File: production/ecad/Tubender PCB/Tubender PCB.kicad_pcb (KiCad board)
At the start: 4 copper layers, 352.2 x 159.2 mm, 262 parts, among them IC1 74HC4050D, IC2 RA8875L3N, IC3 CD4051BM96, IC4 CD4051BM96, J1 640387-2, J10 640387-2, J10 640387-5, J11 640387-8, J12 640387-2, J13 640387-5, J14 640387-3, J15 640387-2, J16 640387-2, J17 640387-2, J18 640387-2, J19 640387-2, J2 640387-5, J20 640387-2, J21 640387-2, J22 640387-2, J23 640387-2, J24 640387-2, J25 640387-2, J26 640387-2, J27 640387-2, J28 640387-2, J29 1-640387-0, J3 640387-5, J30 640387-2, J31 640387-5, J32 USB4110GFA, J33 640387-2, J34 640387-2, J35 640387-3, J37 640387-3, J4 640387-5, J5 640387-2, J5 640387-6, J6 640387-2, J6 640387-6, J7 4-1734592-0, J8 640387-3, J8 640387-6, J9 640387-3, J9 640387-5, Q1 AO3400A, Q2 AO3400A, U1 LMR36520FADDAR, U10 MCP23017-E_SO, U11 SN74AHC1G125DBVR, U12 LM5146RGYR, U13 LM5017SDX/NOPB, U2 ESP32-WROOM-32UE_M113EH6400UH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, U3 MCP23017-E_SO, U5 TPSM265R1V5SILR, U6 CP2102N-A02-GQFN28, Y1 ABM8-20.000MHz-10-B1U-T

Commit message: ok
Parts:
- CBOOT33: value 0.1u -> 0.1uF
- C_BST3, C_VIN1: value 100n -> 100nF
- C_C1: value 6.8n -> 6.8nF
- C_C2: value 312p -> 312pF
- C_C3: value 1n -> 1nF
- C_HF33: value 220n -> 220nF
- C_ILIM1: value 3p -> 3pF
- C_IN2, C_IN33: value 4.7u -> 4.7uF
- C_OUT3: value 10u -> 10uF
- C_OUT33: value 100u -> 100uF
- C_SS1: value 12.5n -> 12.5nF
- C_VCC2: value 2.2u -> 2.2uF
- C_VCC33: value 1u -> 1uF
- L1: value 8.5u -> 8.5uH
- L2: value 12u -> 12uH
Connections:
- U12 pad 22: GND -> (no net)
- U12 pad 23: GND -> (no net)
- U12 pad 24: GND -> (no net)
- U12 pad 25: GND -> (no net)
- U5 pad V: GND -> (no net)
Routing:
- net GND: track 479.9 -> 470.3 mm, vias 87 -> 88
- net ROTATION_ENA+: track 169.1 -> 164.6 mm
- net GPIO_0: track 117.8 -> 115.5 mm, vias 3 -> 2
- net DISPLAY_INT: track 126.3 -> 124.2 mm
- net 24V: track 541.8 -> 540.8 mm
- net TOUCH_XN: track 57.5 -> 56.7 mm
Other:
- board text added: "12V TP"
- board text added: "24V TP"
- board text added: "48V TP"
- board text added: "5V TP"

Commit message: lfg!!!
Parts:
- added G***: LOGO, LOGO, F.Cu at (368.1, 215.0)
- added G***: LOGO, LOGO, F.Cu at (44.2, 79.0)
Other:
- board text added: "(TUBENDER PCB BY NIK AND ETHAN) (SHOUTOUT MAGGIE, NIKI, MATT AND SEAN)"
- board text added: "TUBENDER!!!!!"

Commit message: Duplicate Connectors on Main PCB
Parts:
- removed the J10 at (361.6, 140.1)
- removed the J5 at (361.6, 200.9)
- removed the J6 at (361.6, 170.1)
- removed the J9 at (361.6, 116.7)
- C19, C20, C21, C22, C23, C24, C25, C26, C27, C28, C29, C30, C31, C32, C33: value 500nF -> 490nF
- C_OUT12: value 22u -> 22uF
- moved R8 160.4 mm to (213.4, 94.7)
- moved R18 134.5 mm to (224.2, 90.4), turned to 0 degrees
- moved R7 130.4 mm to (266.4, 90.7), turned to 0 degrees
- moved R17 98.0 mm to (284.2, 90.2), turned to 180 degrees
- moved G*** 55.5 mm to (359.3, 160.2)
- moved R45 43.9 mm to (347.7, 91.7)
- moved R44 40.5 mm to (350.7, 90.8), turned to 0 degrees
- moved R67 26.7 mm to (369.0, 84.3)
- moved G*** 0.51 mm to (44.3, 79.5)
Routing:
- net DIE_LIMIT_2: track 171.0 -> 44.6 mm, vias 3 -> 2
- net DIE_LIMIT_1: track 173.6 -> 48.8 mm, vias 3 -> 2
- net 12V: track 372.5 -> 249.0 mm
- net ADVANCE_LIMIT_1: track 219.2 -> 97.0 mm, vias 3 -> 2
- net ADVANCE_LIMIT_2: track 177.7 -> 56.3 mm, vias 4 -> 2
- net DIE_BEAM: track 191.8 -> 82.9 mm, vias 3 -> 2
- net CHUCK_BEAM: track 184.4 -> 147.5 mm, vias 2 -> 3
- net Net-(J32-CC2): track 33.3 -> 9.88 mm
- net 5V: track 618.8 -> 596.4 mm
- net GND: track 470.3 -> 489.6 mm, vias 88 -> 86

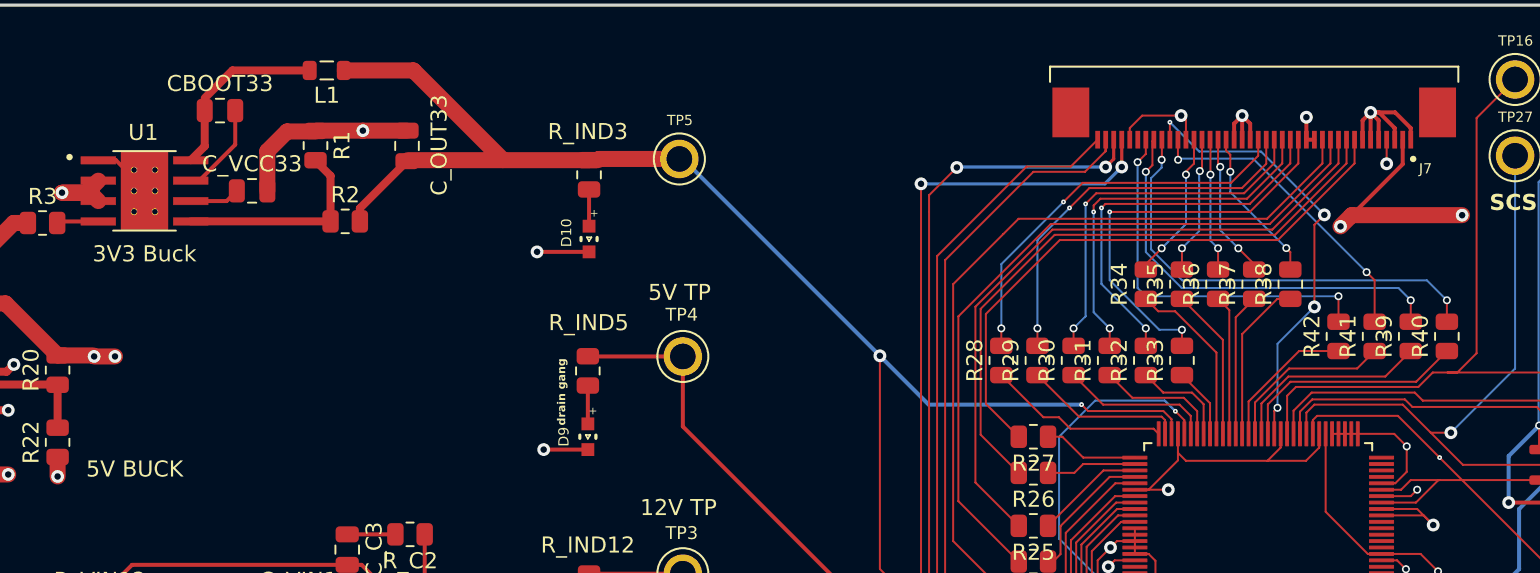
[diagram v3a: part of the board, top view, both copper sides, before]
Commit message: Fixed Blind Vias
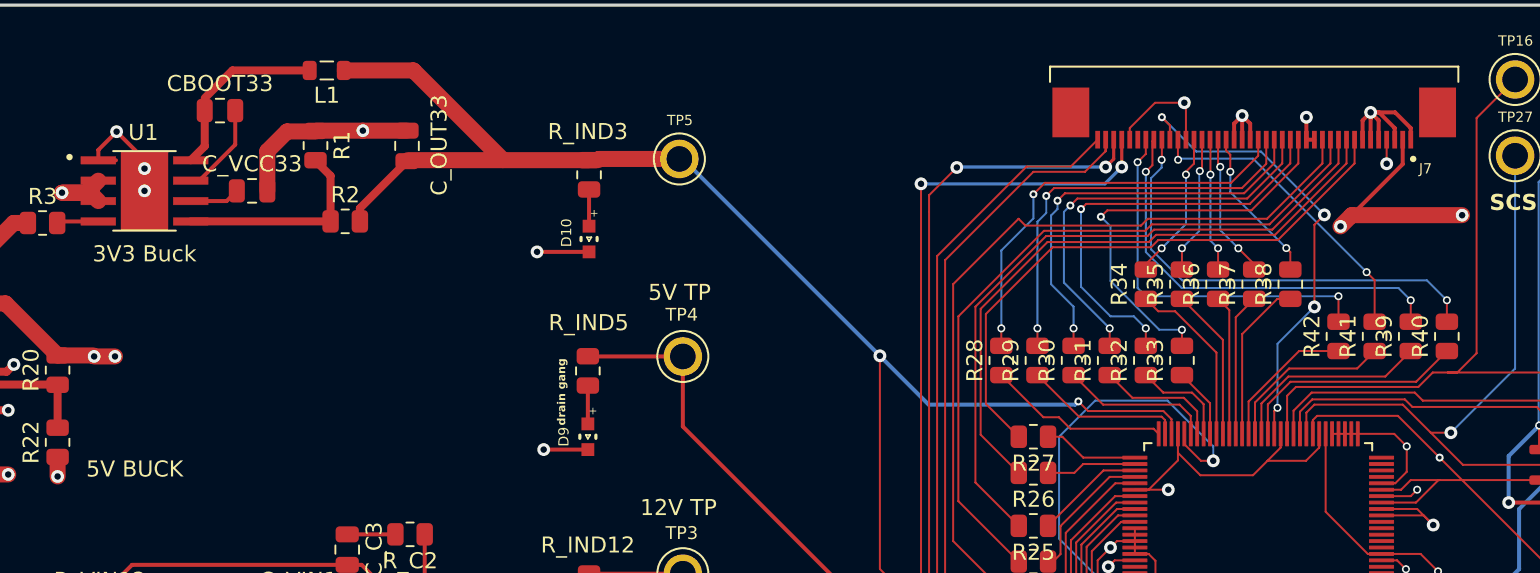
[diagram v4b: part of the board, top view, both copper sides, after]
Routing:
- net GND: track 489.6 -> 494.2 mm, vias 86 -> 89
- net Net-(IC2-CORE_VDD_1): track 145.5 -> 150.0 mm
- net GREEN1: track 24.1 -> 26.7 mm
- net GREEN2: track 23.5 -> 25.8 mm
- net GREEN3: track 23.4 -> 25.7 mm
- net GREEN5: track 24.9 -> 26.3 mm
- net GREEN4: track 24.3 -> 25.6 mm
- net ON/OFF: track 28.0 -> 29.2 mm
- net GREEN0: track 25.5 -> 26.1 mm
